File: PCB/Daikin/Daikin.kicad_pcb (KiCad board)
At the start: 2 copper layers, 13.2 x 16.5 mm, 19 parts, among them J1 1x4, J2 Prog, Q3 PMF250XNEX, U1 ESP32-PICO-MINI-02, U2 LMR16006YDDCR

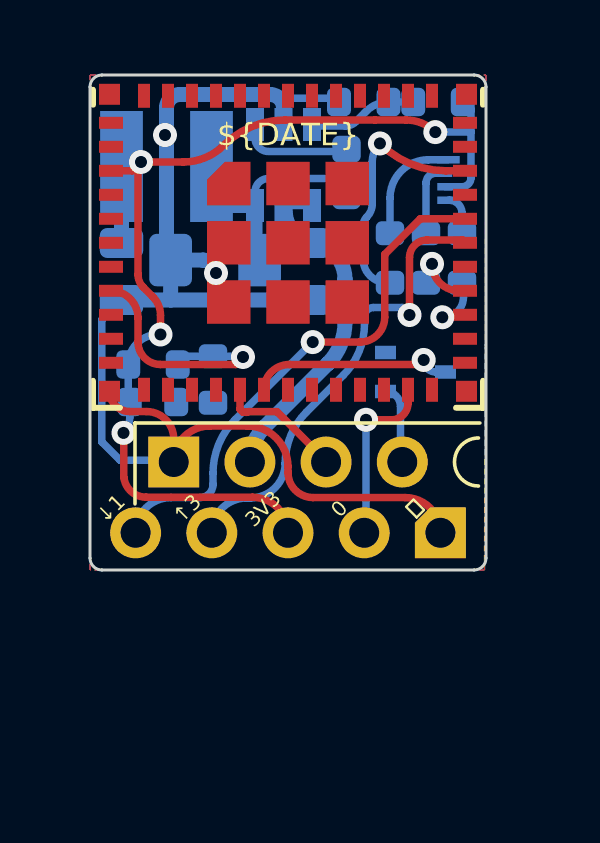
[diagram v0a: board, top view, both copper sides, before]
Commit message: Changed PCB - larger so under pins making harder to fit plug the wrong way. Also changed to 5 pin connector to natch the actual plug to avoid confusion.
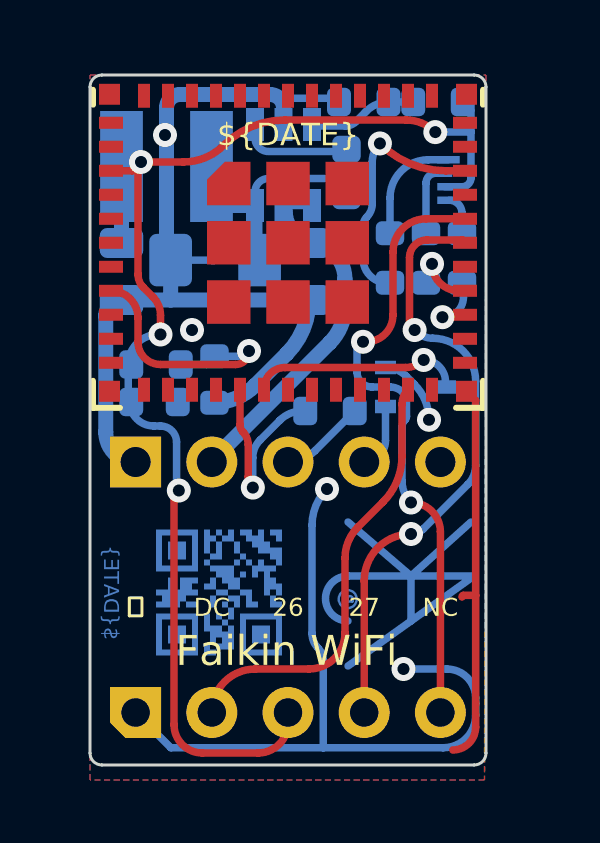
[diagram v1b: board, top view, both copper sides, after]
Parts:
- added Logo1: AJK, RevK:AJK, B.Cu at (103.9, 55.2)
- added R7: 100R, RevK:R_0603, B.Cu at (101.2, 49.7)
- added U3: QR, RevK:QR-DAIKIN, B.Cu at (97.5, 55.8)
- J1: value 1x4 -> 1x5; footprint RevK:JLC-PinHeader_1x04_P2.54mm_Right -> RevK:PinHeader_1x05_P2.54mm_Right
- J2: moved to B.Cu
- moved J2 5.99 mm to (99.8, 59.8), turned to 180 degrees
- moved Q3 0.50 mm to (104.0, 48.9)
- moved R4 0.10 mm to (95.4, 48.1)
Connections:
- J1 pad 3: TX -> Net-(J1-Pad3)
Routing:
- net GND: track 27.6 -> 54.7 mm, vias 2 -> 5
- net Net-(J2-Pad2): track 5.94 -> 14.6 mm, vias 1 -> 0
- net +3.3V: track 34.9 -> 41.8 mm
- net Net-(J2-Pad4): track 15.3 -> 20.4 mm, vias 1 -> 2
- net Net-(J2-Pad5): track 17.5 -> 20.9 mm, vias 1 -> 2
- net Net-(J1-Pad3): track 0.00 -> 2.87 mm
- net TX: track 4.22 -> 6.77 mm, vias 0 -> 1
- net DC: track 10.0 -> 10.6 mm
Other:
- board size 13.2 x 16.5 mm -> 13.2 x 23 mm
- board text added: "NC"
- board text removed: "${DATE}"

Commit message: Added some caps to I/O
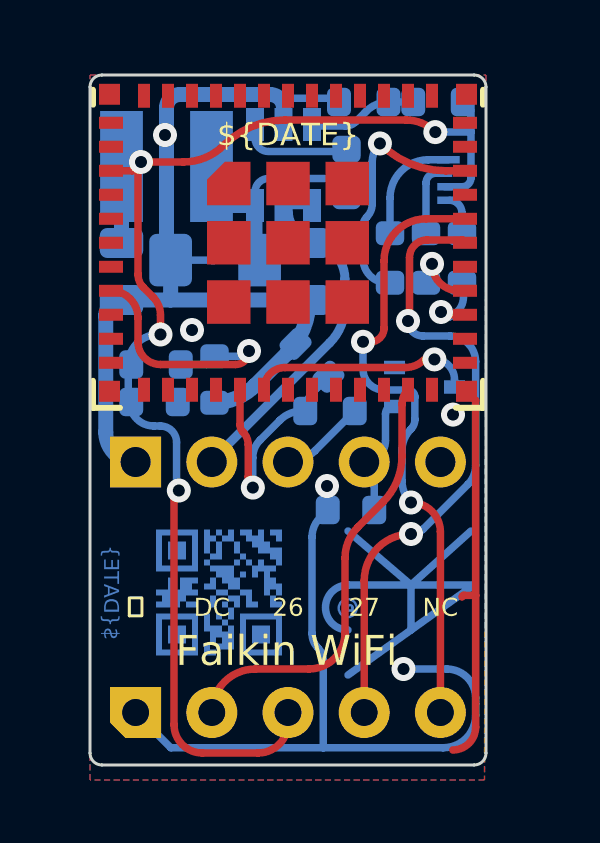
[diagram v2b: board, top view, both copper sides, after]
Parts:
- added C6: 33pF, RevK:C_0603, B.Cu at (100.6, 48.0)
- added C7: 33pF, RevK:C_0603, B.Cu at (101.9, 53.0)
- moved Logo1 0.30 mm to (103.9, 55.5)
- moved Q3 0.30 mm to (104.3, 48.9)
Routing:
- net GND: track 54.7 -> 51.6 mm
- net Net-(J1-Pad4): track 2.23 -> 4.12 mm
- net TX: track 6.77 -> 8.19 mm

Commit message: Tweak artwork
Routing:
- net GND: track 51.6 -> 35.7 mm
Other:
- board text added: "FLASH / DEBUG PORT"
- board text added: "↑"
- board text added: "↓"

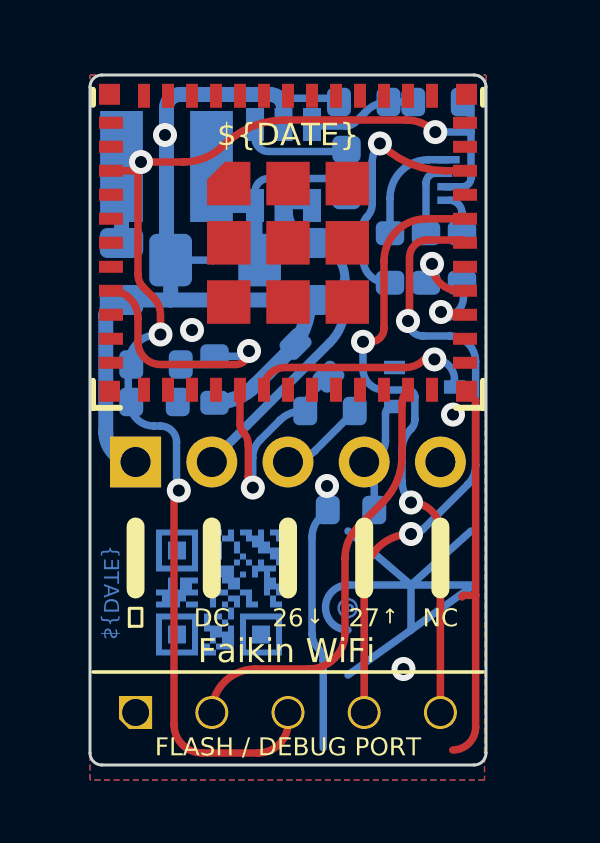
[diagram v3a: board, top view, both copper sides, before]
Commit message: New connector - matching what is on a Daikin
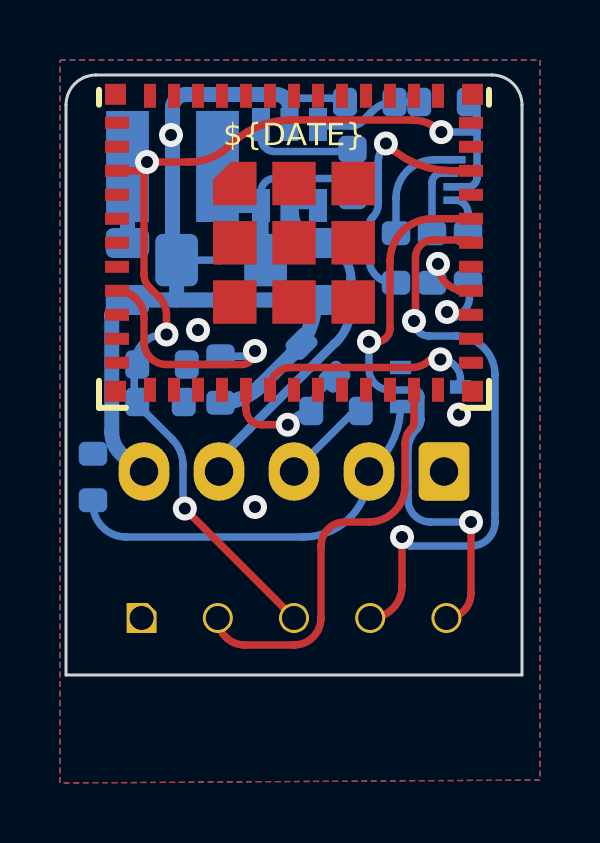
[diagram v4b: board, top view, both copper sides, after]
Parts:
- removed Logo1: AJK, RevK:AJK
- removed U3: QR, RevK:QR-DAIKIN
- J1: footprint RevK:PinHeader_1x05_P2.54mm_Right -> Connector_JST:JST_EH_S5B-EH_1x05_P2.50mm_Horizontal
- moved C7 8.67 mm to (93.3, 51.9), turned to -90 degrees
- moved J1 5.21 mm to (105.0, 51.7), turned to 180 degrees
- moved J2 3.16 mm to (100.0, 56.6)
- moved C1 0.20 mm to (97.5, 48.6)
- moved C2 0.20 mm to (102.0, 41.8)
- moved C3 0.20 mm to (100.7, 45.0)
- moved C4 0.20 mm to (94.5, 45.0)
- moved C5 0.20 mm to (95.5, 49.4)
- moved C6 0.20 mm to (100.8, 48.0)
- moved L1 0.20 mm to (96.0, 41.5)
- moved Q3 0.20 mm to (104.5, 48.9)
- moved R2 0.20 mm to (103.4, 44.6)
- moved R3 0.20 mm to (105.8, 44.6)
- moved R5 0.20 mm to (105.0, 39.4)
- moved R6 0.20 mm to (102.5, 39.4)
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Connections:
- J1 pad 1: GND -> unconnected-(J1-Pad1)
- J1 pad 2: DC -> Net-(C7-Pad2)
- J1 pad 4: Net-(C7-Pad2) -> DC
- J1 pad 5: unconnected-(J1-Pad5) -> GND
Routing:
- net GND: track 35.7 -> 14.5 mm, vias 5 -> 4
- net Net-(C7-Pad2): track 4.12 -> 13.5 mm
- net +3.3V: track 41.5 -> 34.1 mm
- net TX: track 8.19 -> 4.67 mm
- net Net-(J2-Pad5): track 21.0 -> 19.4 mm
- net Net-(J2-Pad4): track 20.9 -> 20.0 mm
- net Net-(J2-Pad2): track 14.6 -> 13.9 mm
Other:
- board size 13.2 x 23 mm -> 15.2 x 20 mm
- board text added: "Faikin - www.me.uk"
- board text removed: "FLASH / DEBUG PORT"
- board text removed: "Faikin WiFi"
